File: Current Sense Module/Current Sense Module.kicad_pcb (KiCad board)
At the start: 2 copper layers, 14 parts, among them J1 Conn_01x03_Male, J2 Conn_01x03_Male, J3 Conn_01x05_Male, U1 TLC2272

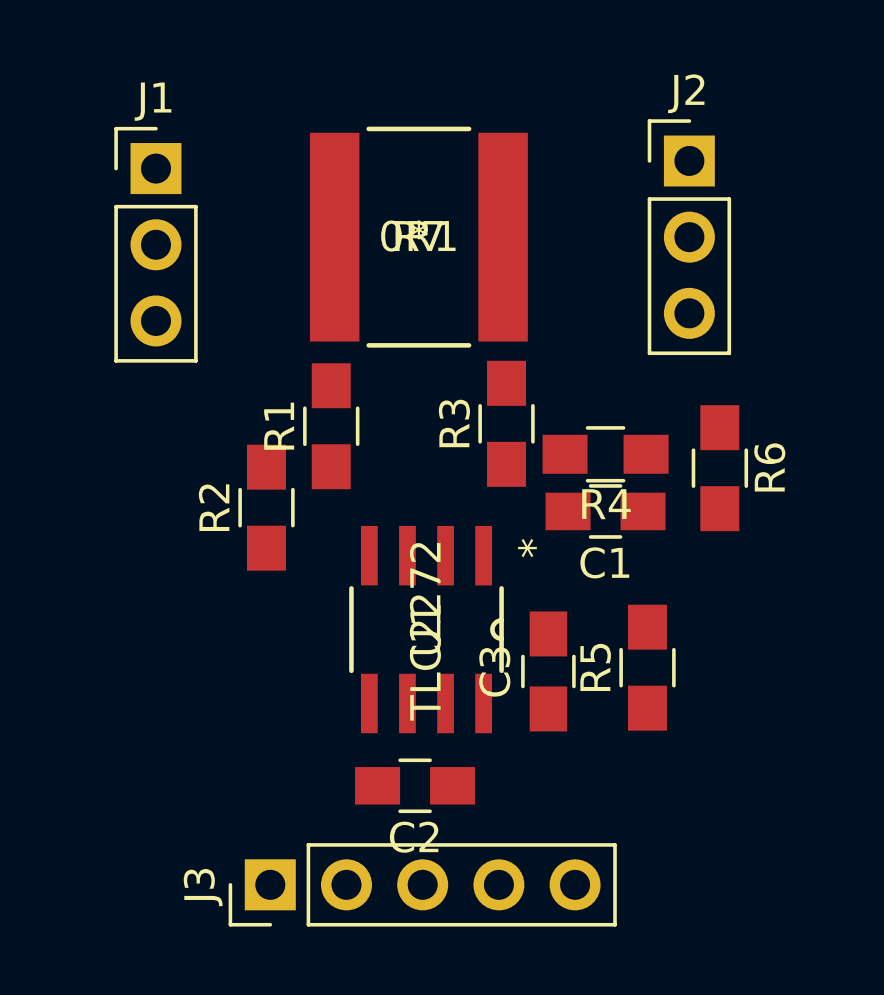
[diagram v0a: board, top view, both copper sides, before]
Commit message: Completed PCB layout
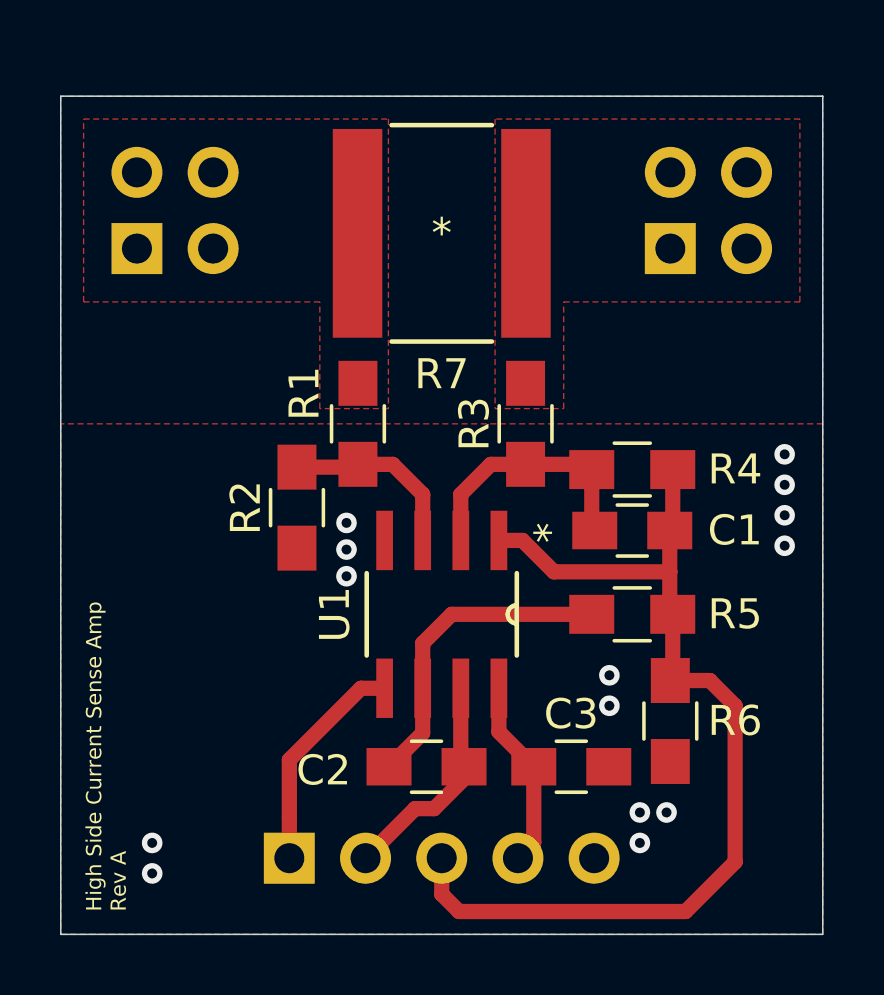
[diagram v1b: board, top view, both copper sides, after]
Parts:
- J1, J2: value Conn_01x03_Male -> Conn_01x04_Male; footprint Pin_Headers:Pin_Header_Straight_1x03_Pitch2.54mm -> Pin_Headers:Pin_Header_Straight_2x02_Pitch2.54mm; moved to B.Cu
- J3: moved to B.Cu
- moved R6 8.59 mm to (121.9, 84.3), turned to 90 degrees
- moved C3 3.27 mm to (118.6, 85.9), turned to 0 degrees
- moved J2 2.99 mm to (121.9, 68.6)
- moved J1 2.74 mm to (104.1, 68.6)
- moved R5 1.85 mm to (120.7, 80.8), turned to 0 degrees
- moved C1 1.09 mm to (120.7, 78.0)
- moved J3 1.09 mm to (109.2, 88.9), turned to 270 degrees
- moved R4 1.02 mm to (120.7, 75.9)
- moved R2 1.02 mm to (109.5, 77.2)
- moved R1 0.89 mm to (111.5, 74.4)
- moved R7 0.77 mm to (114.3, 68.1)
- moved C2 0.74 mm to (113.8, 85.9)
- moved U1 0.72 mm to (114.3, 80.8)
- moved R3 0.63 mm to (117.1, 74.4)
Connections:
- J3 pad 1: GND -> /Cmp_Ref_In
- J3 pad 2: VCC -> /Cmp_Out
- J3 pad 4: /Cmp_Ref_In -> VCC
- J3 pad 5: /Cmp_Out -> GND
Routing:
- net /Diff_Out: track 0.00 -> 32.9 mm
- net Net-(C2-Pad2): track 0.00 -> 10.6 mm
- net Net-(C1-Pad2): track 0.00 -> 8.46 mm
- net /Cmp_Ref_In: track 0.00 -> 7.44 mm
- net /Cmp_Out: track 0.00 -> 7.44 mm
- net VCC: track 0.00 -> 6.36 mm
- net Net-(R1-Pad1): track 0.00 -> 6.18 mm
- net GND: vias 0 -> 14
- added copper zone on F.Cu, net /Bus_Voltage
- added copper zone on F.Cu, net /Load
- added copper zone on B.Cu, net GND
- added copper zone on F.Cu, net GND
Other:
- board outline added: 25.4 x 27.9 mm
- net class Default: clearance 0.2 -> 0.1524; trace_width 0.25 -> 0.1524; via_dia 0.8 -> 0.6858; via_drill 0.4 -> 0.3302
- net class VCC added: clearance 0.254, trace_width 0.508, via_dia 1.016, via_drill 0.508
- rule pad_to_mask_clearance: 0.051 -> 0.0508
- rule solder_mask_min_width: 0.25 -> 0.101
- rule trace_clearance: 0.2 -> 0.1524
- rule trace_min: 0.2 -> 0.1524
- rule via_min_drill: 0.3 -> 0.254
- rule via_min_size: 0.4 -> 0.508
- board text added: "High Side Current Sense Amp Rev A"

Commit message: PCB tweal
Inverted pin headers and edited silk screen.
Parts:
- J1, J2, J3: moved to F.Cu
- moved J1 2.54 mm to (104.1, 66.0)
- moved J2 2.54 mm to (121.9, 66.0)
- turned J3 to 90 degrees
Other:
- board text added: "Cmp"
- board text added: "Diff"
- board text added: "Gnd"
- board text added: "Ref"
- board text added: "Vcc"

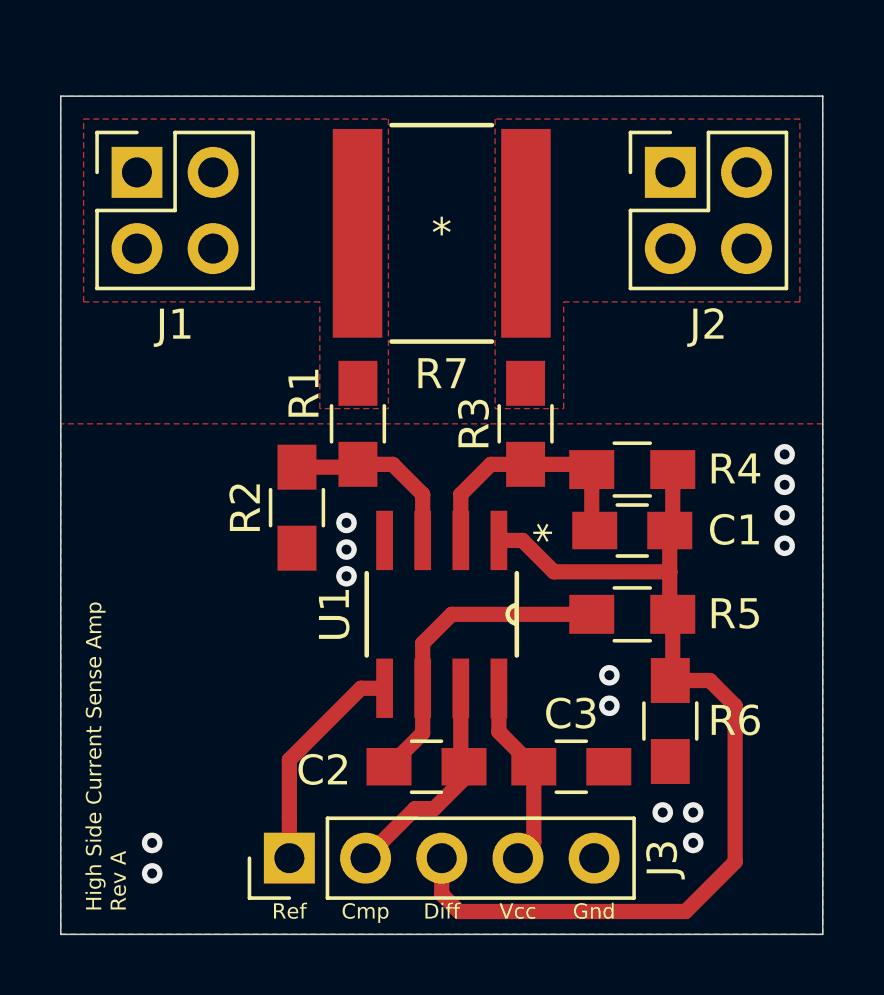
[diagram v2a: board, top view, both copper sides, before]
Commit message: Rev B
Added thermal jumpers. Brought out inputs of the second op-amp to header. Added BOM.
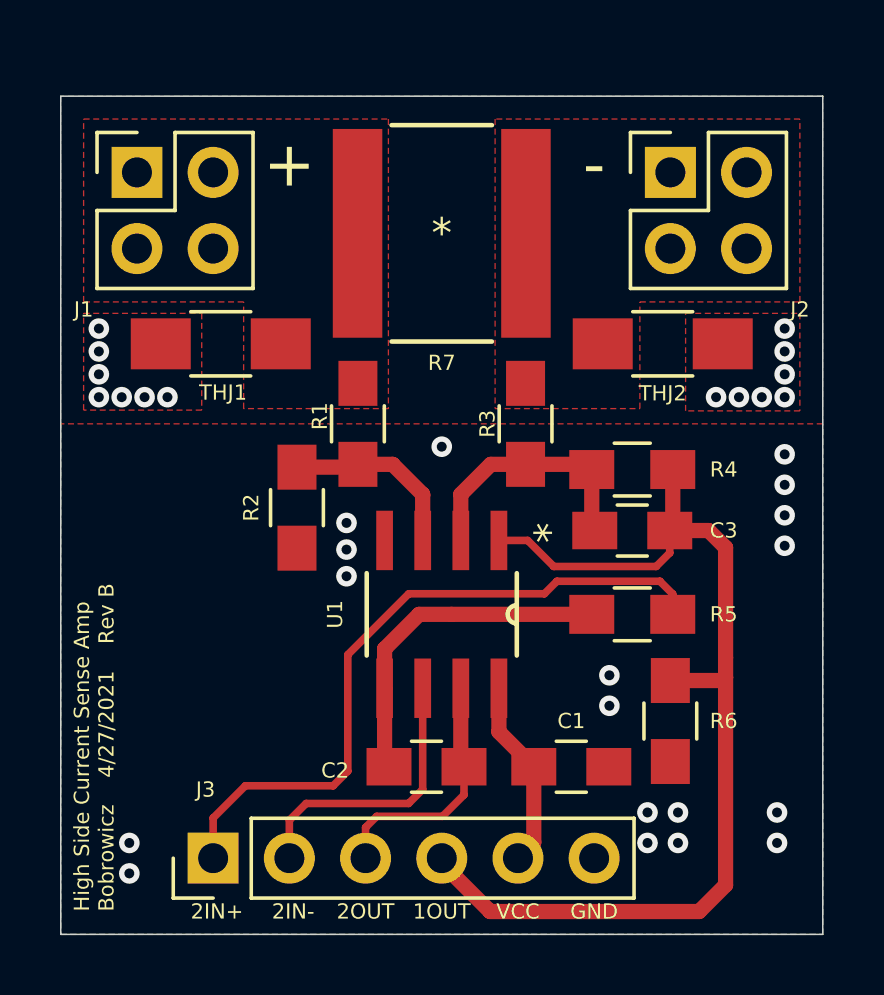
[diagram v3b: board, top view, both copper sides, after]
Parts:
- added THJ1: R, Resistors_SMD:R_1206_HandSoldering, F.Cu at (106.9, 71.8)
- added THJ2: R, Resistors_SMD:R_1206_HandSoldering, F.Cu at (121.7, 71.8)
- C1: renamed from C3; value 0.1uF -> 0.1u
- C2: value 1nF -> 330p
- C3: renamed from C1; value 1nF -> 0p
- J3: value Conn_01x05_Male -> Conn_01x06_Male; footprint Pin_Headers:Pin_Header_Straight_1x05_Pitch2.54mm -> Pin_Headers:Pin_Header_Straight_1x06_Pitch2.54mm
- R1, R3: value 1k -> 10k 0.1%
- R2: value 20k -> 100k 0.1%
- R4: value 20k -> 100k 0.1 %
- R7: value 0R1 -> 0R1 0.5%
- U1: value TLC2272 -> OPA2990
- moved J3 2.54 mm to (106.7, 88.9)
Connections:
- net Net-(C1-Pad2) renamed /1IN-
- net Net-(R1-Pad1) renamed /1IN+
- C2 pad 1: /Cmp_Out -> /2OUT
- C3 pad 1: /Diff_Out -> /1OUT
- J3 pad 1: /Cmp_Ref_In -> /2IN+
- J3 pad 2: /Cmp_Out -> /2IN-
- J3 pad 3: /Diff_Out -> /2OUT
- J3 pad 4: VCC -> /1OUT
- J3 pad 5: GND -> VCC
- R4 pad 1: /Diff_Out -> /1OUT
- R5 pad 2: /Diff_Out -> /2IN+
- R6 pad 2: /Diff_Out -> /1OUT
- U1 pad 1: /Diff_Out -> /1OUT
- U1 pad 5: /Cmp_Ref_In -> Net-(C2-Pad2)
- U1 pad 6: Net-(C2-Pad2) -> /2IN-
- U1 pad 7: /Cmp_Out -> /2OUT
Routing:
- net /1OUT: track 0.00 -> 35.0 mm
- net /Diff_Out: track 32.9 -> 0.00 mm
- net /2IN+: track 0.00 -> 23.1 mm
- net /2IN-: track 0.00 -> 9.51 mm
- net /2OUT: track 0.00 -> 8.35 mm
- net /Cmp_Ref_In: track 7.44 -> 0.00 mm
- net /Cmp_Out: track 7.44 -> 0.00 mm
- net Net-(C2-Pad2): track 10.6 -> 11.4 mm
- net GND: vias 14 -> 32
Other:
- board text added: "+"
- board text added: "-"
- board text added: "1OUT"
- board text added: "2IN+"
- board text added: "2IN-"
- board text added: "2OUT"
- board text added: "GND"
- board text added: "High Side Current Sense Amp Bobrowicz 4/27/2021 Rev B"
- board text added: "VCC"
- board text removed: "Cmp"
- board text removed: "Diff"
- board text removed: "Gnd"
- board text removed: "High Side Current Sense Amp Rev A"
- board text removed: "Ref"
- board text removed: "Vcc"
